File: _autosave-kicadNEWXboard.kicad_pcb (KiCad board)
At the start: 2 copper layers, 208 x 120.7 mm, 112 parts, among them SW1 SW_Push, U1 ATmega32U4-AU, Y1 16MHz

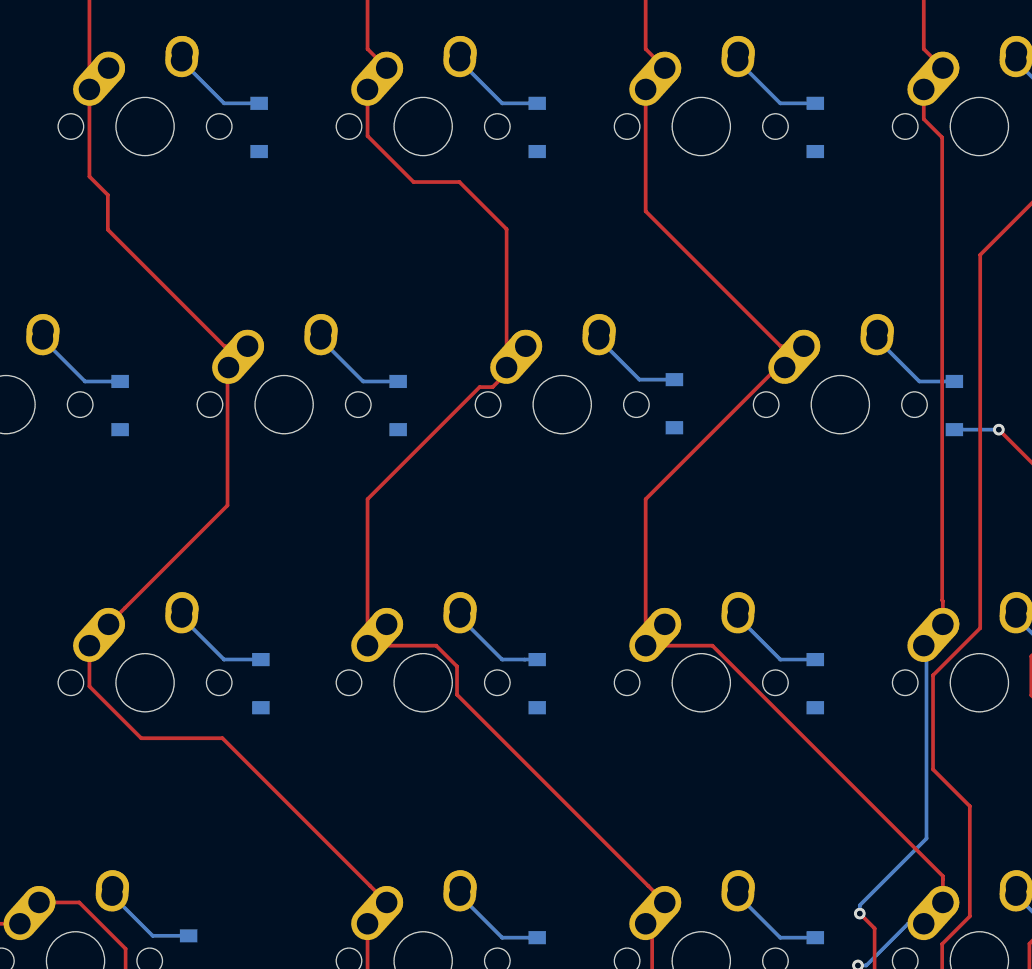
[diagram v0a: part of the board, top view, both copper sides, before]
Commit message: added submodule marbastlib
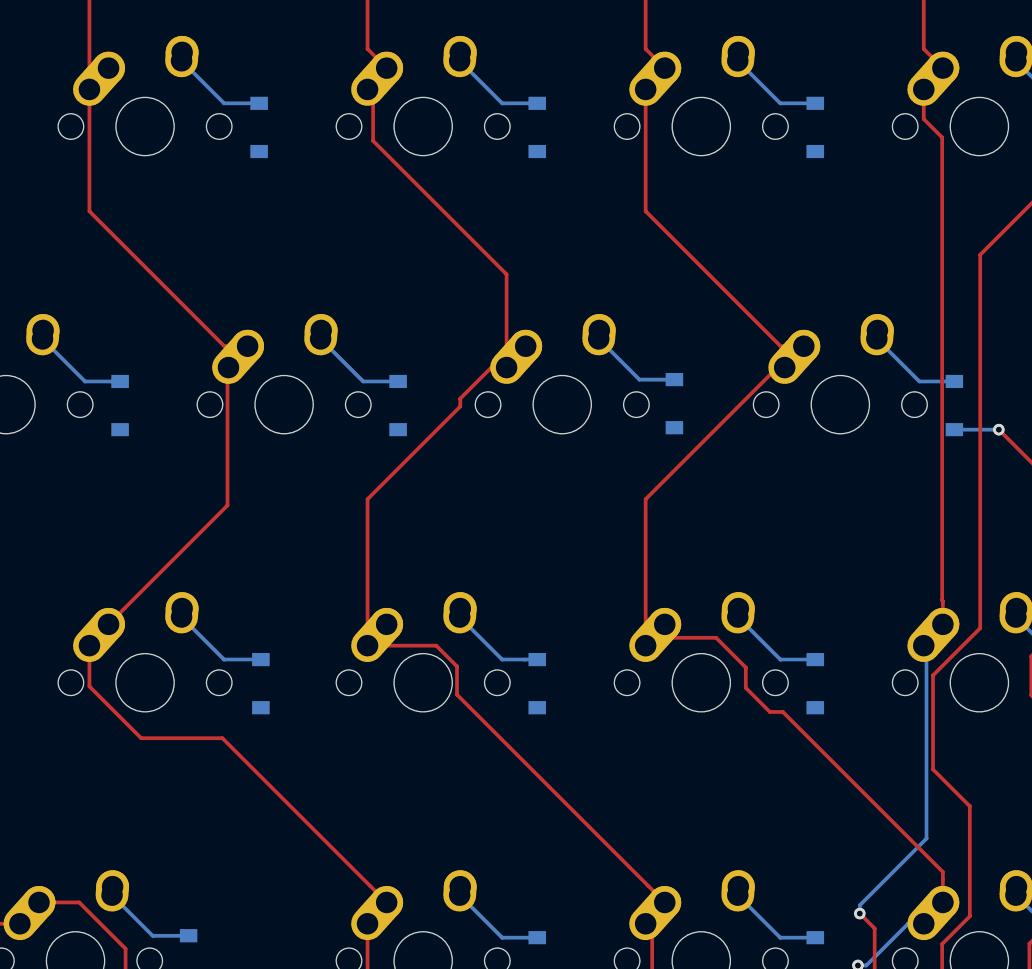
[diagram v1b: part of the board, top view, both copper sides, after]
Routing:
- net COL7: track 116.0 -> 114.3 mm
- net COL8: track 121.3 -> 122.7 mm
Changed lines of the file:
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@@
     (thickness 1.6)
     (drawings 10)
-    (tracks 742)
+    (tracks 744)
     (zones 0)
     (modules 112)
@@
       (creategerberjobfile false)
       (excludeedgelayer true)
-      (linewidth 0.100000)
+      (linewidth 0.020000)
       (plotframeref false)
       (viasonmask false)
@@
   (segment (start 188.668011 122.374011) (end 193.218 126.924) (width 0.254) (layer B.Cu) (net 84))
   (segment (start 154.94 33.17875) (end 154.94 52.22875) (width 0.254) (layer F.Cu) (net 85))
-  (segment (start 164.18401 69.81875) (end 165.775 69.81875) (width 0.254) (layer F.Cu) (net 85))
-  (segment (start 156.200499 61.835239) (end 164.18401 69.81875) (width 0.254) (layer F.Cu) (net 85))
-  (segment (start 156.200499 59.458249) (end 156.200499 61.835239) (width 0.254) (layer F.Cu) (net 85))
-  (segment (start 154.94 58.19775) (end 156.200499 59.458249) (width 0.254) (layer F.Cu) (net 85))
-  (segment (start 154.94 52.22875) (end 154.94 58.19775) (width 0.254) (layer F.Cu) (net 85))
   (segment (start 157.374999 87.743751) (end 156.25 88.86875) (width 0.254) (layer F.Cu) (net 85))
   (segment (start 164.397001 80.721749) (end 157.374999 87.743751) (width 0.254) (layer F.Cu) (net 85))
@@
   (segment (start 194.018 128.76125) (end 194.018 127.081932) (width 0.254) (layer B.Cu) (net 85))
   (segment (start 194.018 127.081932) (end 188.856068 121.92) (width 0.254) (layer B.Cu) (net 85))
+  (segment (start 164.18401 69.81875) (end 165.775 69.81875) (width 0.254) (layer F.Cu) (net 85))
+  (segment (start 154.94 52.22875) (end 154.94 60.57474) (width 0.254) (layer F.Cu) (net 85))
+  (segment (start 154.94 60.57474) (end 164.18401 69.81875) (width 0.254) (layer F.Cu) (net 85))
   (segment (start 173.99 49.45875) (end 175.3 50.76875) (width 0.254) (layer F.Cu) (net 86))
   (segment (start 173.99 33.17875) (end 173.99 49.45875) (width 0.254) (layer F.Cu) (net 86))
-  (segment (start 183.515 61.800148) (end 183.515 71.27875) (width 0.254) (layer F.Cu) (net 86))
-  (segment (start 180.284101 58.569249) (end 183.515 61.800148) (width 0.254) (layer F.Cu) (net 86))
-  (segment (start 177.144161 58.569249) (end 180.284101 58.569249) (width 0.254) (layer F.Cu) (net 86))
-  (segment (start 173.99 55.415088) (end 177.144161 58.569249) (width 0.254) (layer F.Cu) (net 86))
-  (segment (start 173.99 52.22875) (end 173.99 55.415088) (width 0.254) (layer F.Cu) (net 86))
-  (segment (start 173.99 80.294788) (end 173.99 90.32875) (width 0.254) (layer F.Cu) (net 86))
-  (segment (start 181.668039 72.616749) (end 173.99 80.294788) (width 0.254) (layer F.Cu) (net 86))
-  (segment (start 182.558001 72.616749) (end 181.668039 72.616749) (width 0.254) (layer F.Cu) (net 86))
-  (segment (start 183.515 71.65975) (end 182.558001 72.616749) (width 0.254) (layer F.Cu) (net 86))
-  (segment (start 183.515 71.27875) (end 183.515 71.65975) (width 0.254) (layer F.Cu) (net 86))
   (segment (start 193.225001 106.793751) (end 194.35 107.91875) (width 0.254) (layer F.Cu) (net 86))
   (segment (start 180.120901 93.689651) (end 193.225001 106.793751) (width 0.254) (layer F.Cu) (net 86))
@@
   (segment (start 193.4845 125.906364) (end 194.818 127.239864) (width 0.254) (layer B.Cu) (net 86))
   (segment (start 193.4845 115.28425) (end 193.4845 125.906364) (width 0.254) (layer B.Cu) (net 86))
+  (segment (start 183.515 64.897) (end 183.515 71.27875) (width 0.254) (layer F.Cu) (net 86))
+  (segment (start 174.371 55.753) (end 183.515 64.897) (width 0.254) (layer F.Cu) (net 86))
+  (segment (start 173.99 52.22875) (end 174.371 52.60975) (width 0.254) (layer F.Cu) (net 86))
+  (segment (start 174.371 52.60975) (end 174.371 55.753) (width 0.254) (layer F.Cu) (net 86))
+  (segment (start 173.99 80.294788) (end 173.99 90.32875) (width 0.254) (layer F.Cu) (net 86))
+  (segment (start 180.34 73.944788) (end 173.99 80.294788) (width 0.254) (layer F.Cu) (net 86))
+  (segment (start 180.34 73.406) (end 180.34 73.944788) (width 0.254) (layer F.Cu) (net 86))
+  (segment (start 183.515 71.27875) (end 182.46725 71.27875) (width 0.254) (layer F.Cu) (net 86))
+  (segment (start 182.46725 71.27875) (end 180.34 73.406) (width 0.254) (layer F.Cu) (net 86))
   (segment (start 193.04 49.45875) (end 194.35 50.76875) (width 0.254) (layer F.Cu) (net 87))
   (segment (start 193.04 33.17875) (end 193.04 49.45875) (width 0.254) (layer F.Cu) (net 87))
@@
   (segment (start 202.056038 71.27875) (end 193.04 80.294788) (width 0.254) (layer F.Cu) (net 87))
   (segment (start 202.565 71.27875) (end 202.056038 71.27875) (width 0.254) (layer F.Cu) (net 87))
-  (segment (start 213.4 106.32776) (end 213.4 107.91875) (width 0.254) (layer F.Cu) (net 87))
-  (segment (start 213.4 106.117712) (end 213.4 106.32776) (width 0.254) (layer F.Cu) (net 87))
-  (segment (start 197.611038 90.32875) (end 213.4 106.117712) (width 0.254) (layer F.Cu) (net 87))
-  (segment (start 193.04 90.32875) (end 197.611038 90.32875) (width 0.254) (layer F.Cu) (net 87))
   (via (at 206.6925 115.53825) (size 0.8) (drill 0.4) (layers F.Cu B.Cu) (net 87))
   (via (at 207.5815 112.23625) (size 0.8) (drill 0.4) (layers F.Cu B.Cu) (net 87))
@@
   (segment (start 206.6925 115.53825) (end 205.00975 115.53825) (width 0.254) (layer B.Cu) (net 87))
   (segment (start 205.00975 115.53825) (end 195.618 124.93) (width 0.254) (layer B.Cu) (net 87))
+  (segment (start 213.4 106.32776) (end 213.4 107.91875) (width 0.254) (layer F.Cu) (net 87))
+  (segment (start 213.4 105.831) (end 213.4 106.32776) (width 0.254) (layer F.Cu) (net 87))
+  (segment (start 202.438 94.869) (end 213.4 105.831) (width 0.254) (layer F.Cu) (net 87))
+  (segment (start 193.57975 89.789) (end 197.866 89.789) (width 0.254) (layer F.Cu) (net 87))
+  (segment (start 193.04 90.32875) (end 193.57975 89.789) (width 0.254) (layer F.Cu) (net 87))
+  (segment (start 197.866 89.789) (end 199.898 91.821) (width 0.254) (layer F.Cu) (net 87))
+  (segment (start 199.898 91.821) (end 199.898 93.218) (width 0.254) (layer F.Cu) (net 87))
+  (segment (start 199.898 93.218) (end 201.549 94.869) (width 0.254) (layer F.Cu) (net 87))
+  (segment (start 201.549 94.869) (end 202.438 94.869) (width 0.254) (layer F.Cu) (net 87))
   (segment (start 212.09 49.45875) (end 213.4 50.76875) (width 0.254) (layer F.Cu) (net 88))
   (segment (start 212.09 33.17875) (end 212.09 49.45875) (width 0.254) (layer F.Cu) (net 88))
